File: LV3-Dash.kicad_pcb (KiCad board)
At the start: 2 copper layers, 88.9 x 50 mm, 95 parts, among them J1 Conn_01x05_MountingPin, J10 Conn_01x01, J2 USB_C_Receptacle_USB2.0_16P, J3 Conn_01x04_MountingPin, J4 MSD-11-A, J5 Conn_01x05_Pin, J7 62684-401100AHLF, J8 FTSH-105-01-L-DV-K-A, U1 STM32H743VITx, U2 TJA1051T-3, U3 AP3032KTR, U4 LMR51625YDDCR, U5 TLV74033PDBVR, U6 TLV74033PDBVR, Y1 Crystal_GND24

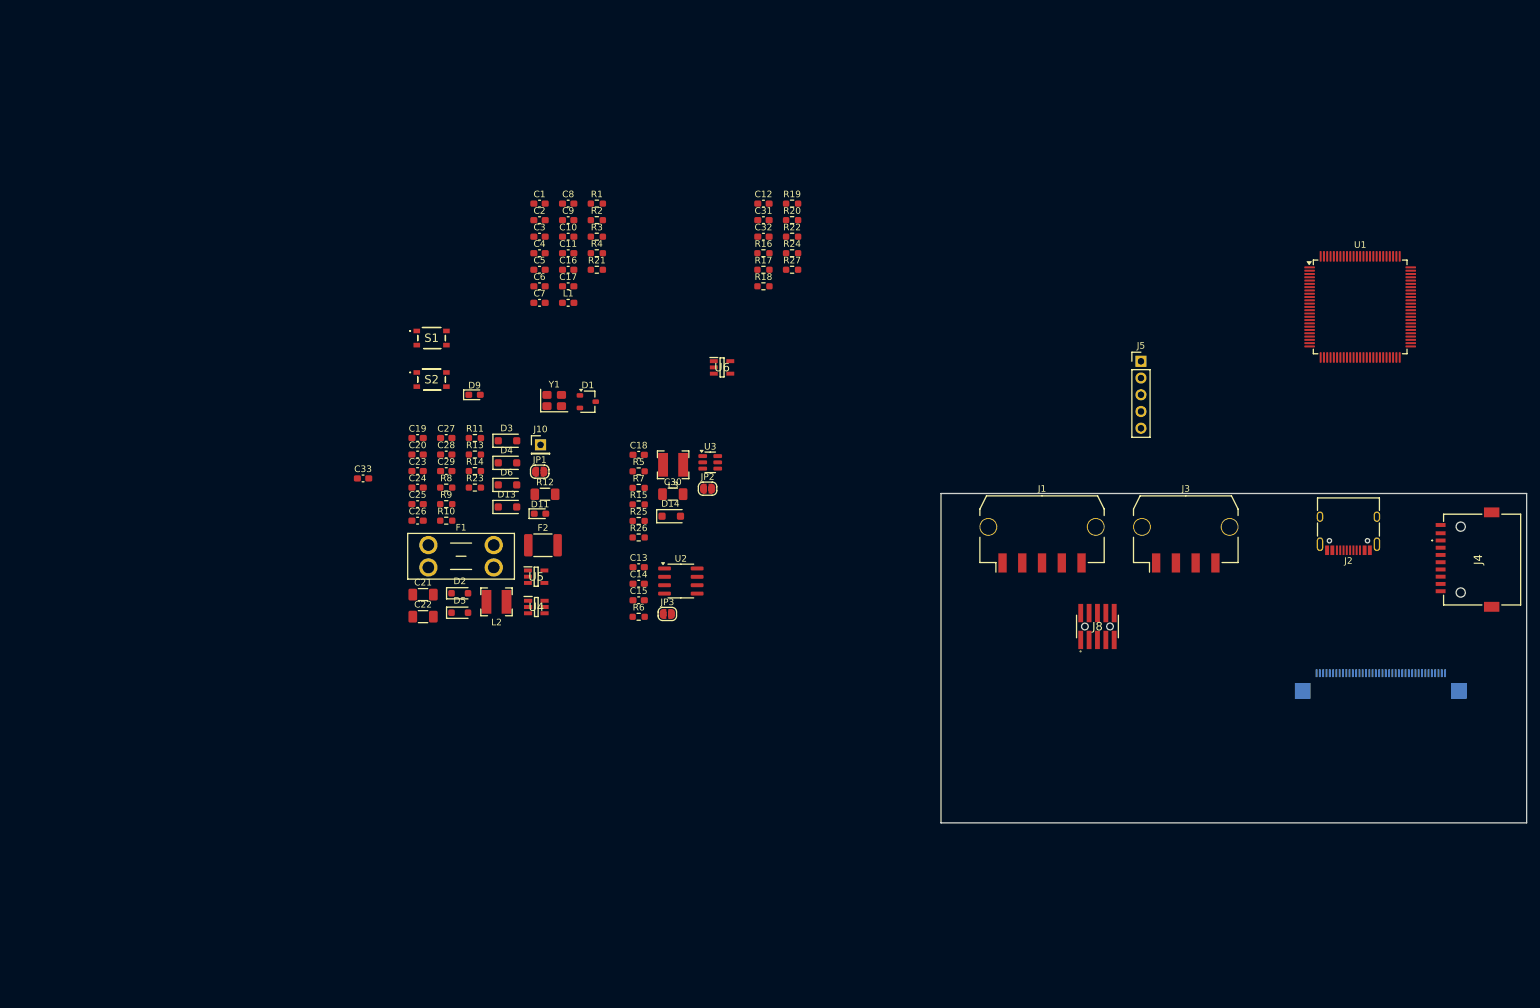
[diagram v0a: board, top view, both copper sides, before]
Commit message: initial dimensions and placement
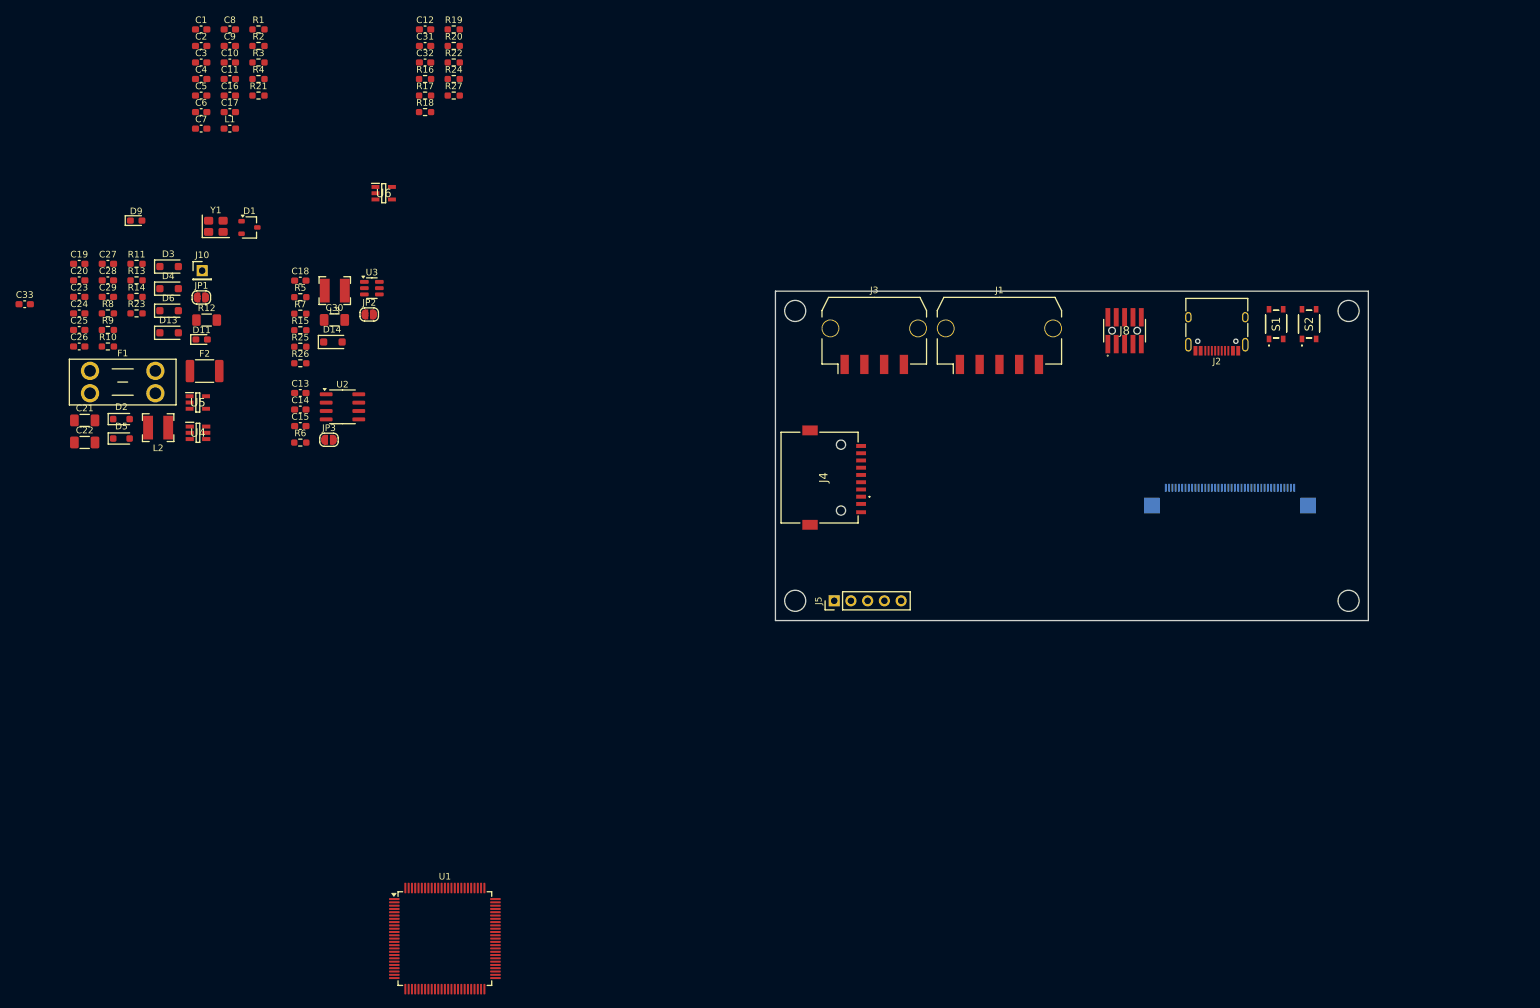
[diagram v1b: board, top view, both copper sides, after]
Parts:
- moved U1 168.8 mm to (99.8, 168.3)
- moved S2 133.5 mm to (231.0, 75.0), turned to 90 degrees
- moved S1 128.2 mm to (226.0, 75.0), turned to 90 degrees
- moved J4 100.9 mm to (156.9, 98.3), turned to -90 degrees
- moved J5 59.1 mm to (158.9, 117.0), turned to 90 degrees
- moved C11 57.8 mm to (67.2, 37.8)
- moved C12 57.8 mm to (96.8, 30.3)
- moved C14 57.8 mm to (77.9, 88.0)
- moved C8 57.8 mm to (67.2, 30.3)
- moved L1 57.8 mm to (67.2, 45.3)
- moved L2 57.8 mm to (56.3, 90.7)
- moved R13 57.8 mm to (53.0, 68.4)
- moved R16 57.8 mm to (96.8, 37.8)
- moved C10 57.8 mm to (67.2, 35.3)
- moved C13 57.8 mm to (77.9, 85.5)
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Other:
- board size 88.9 x 50 mm -> 90 x 50 mm

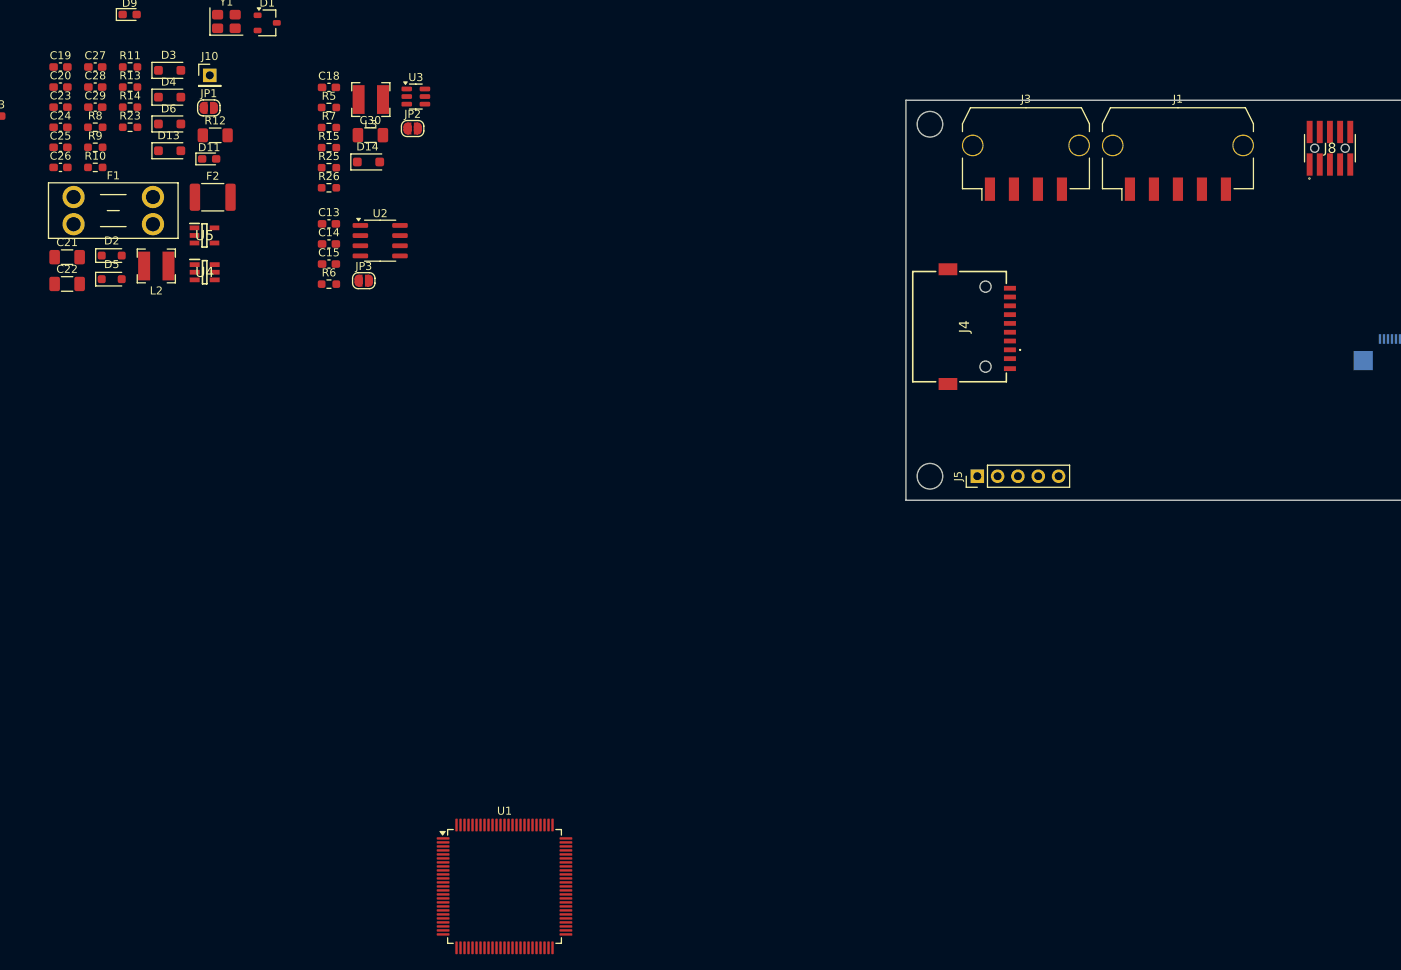
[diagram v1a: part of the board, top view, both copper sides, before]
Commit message: fix swd connector orientation, modify 12v input
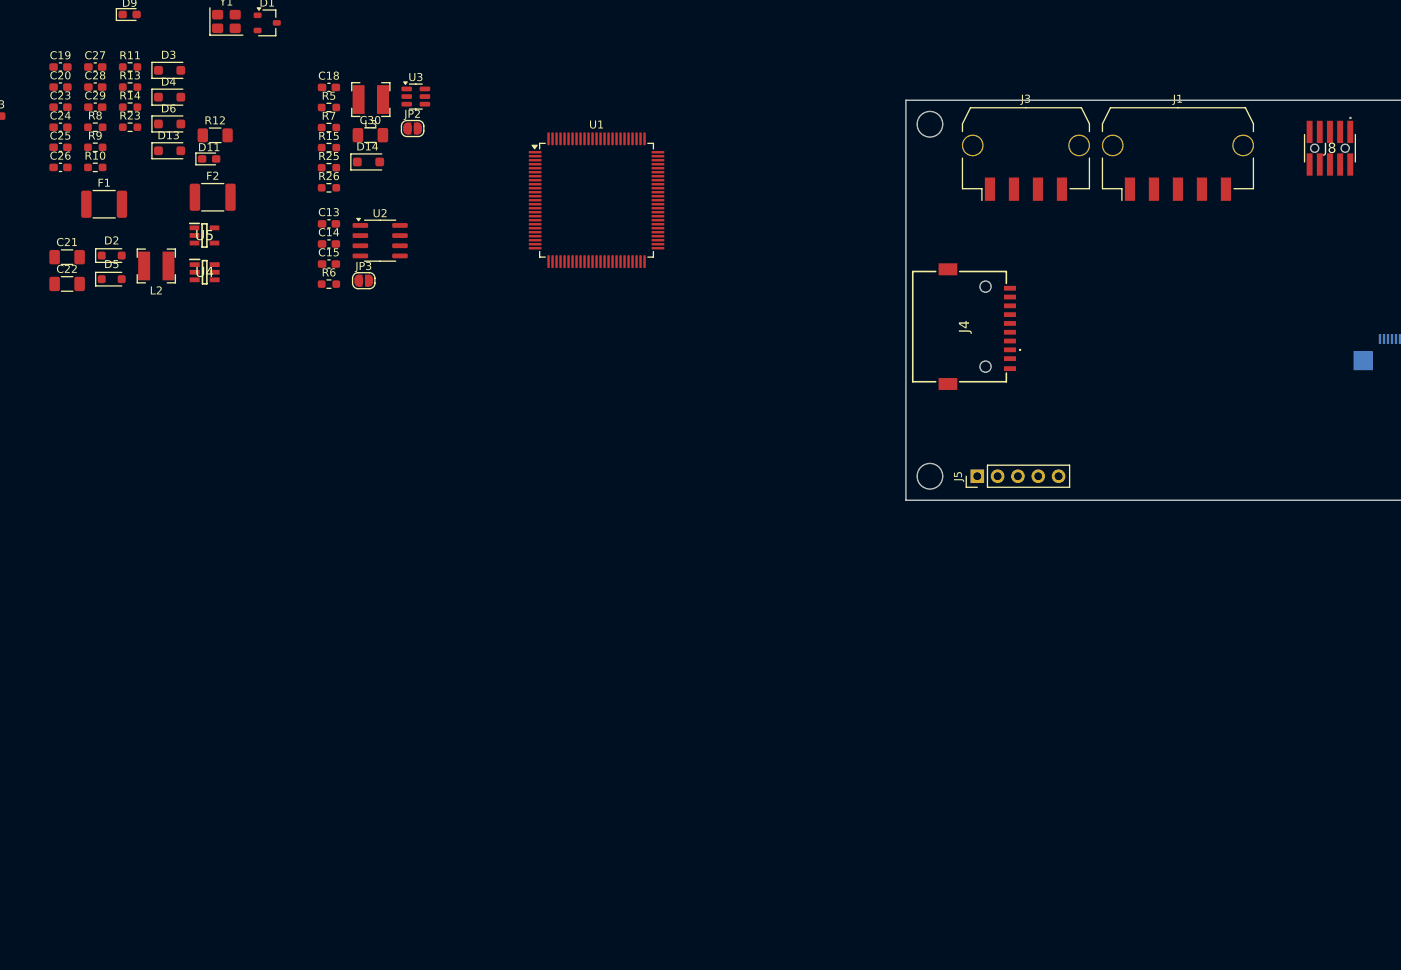
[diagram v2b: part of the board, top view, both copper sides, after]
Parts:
- removed J10: Conn_01x01, Connector_PinHeader_2.54mm:PinHeader_1x01_P2.54mm_Vertical
- removed JP1: SolderJumper_2_Open, Jumper:SolderJumper-2_P1.3mm_Open_RoundedPad1.0x1.5mm
- F1: value Fuse -> Polyfuse; footprint Fuse:Fuseholder_Blade_Mini_Keystone_3568 -> Fuse:Fuse_1812_4532Metric_Pad1.30x3.40mm_HandSolder
- moved U1 86.5 mm to (111.3, 82.5)
- moved F1 3.92 mm to (49.8, 83.0)
- turned J8 to 180 degrees
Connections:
- D13 pad 2: Net-(D13-A) -> +12V

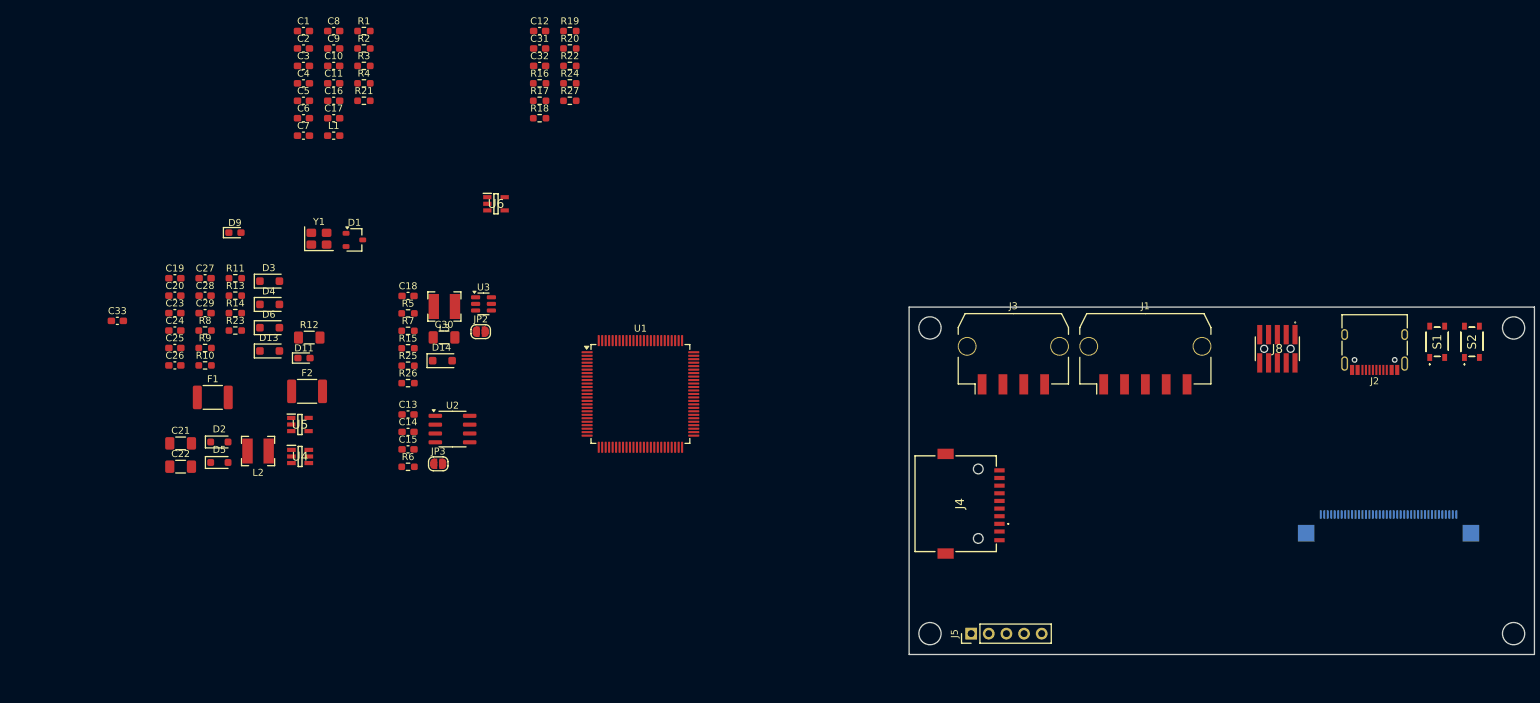
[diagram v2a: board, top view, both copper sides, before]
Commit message: basic layout organization, fix +VDDA typo
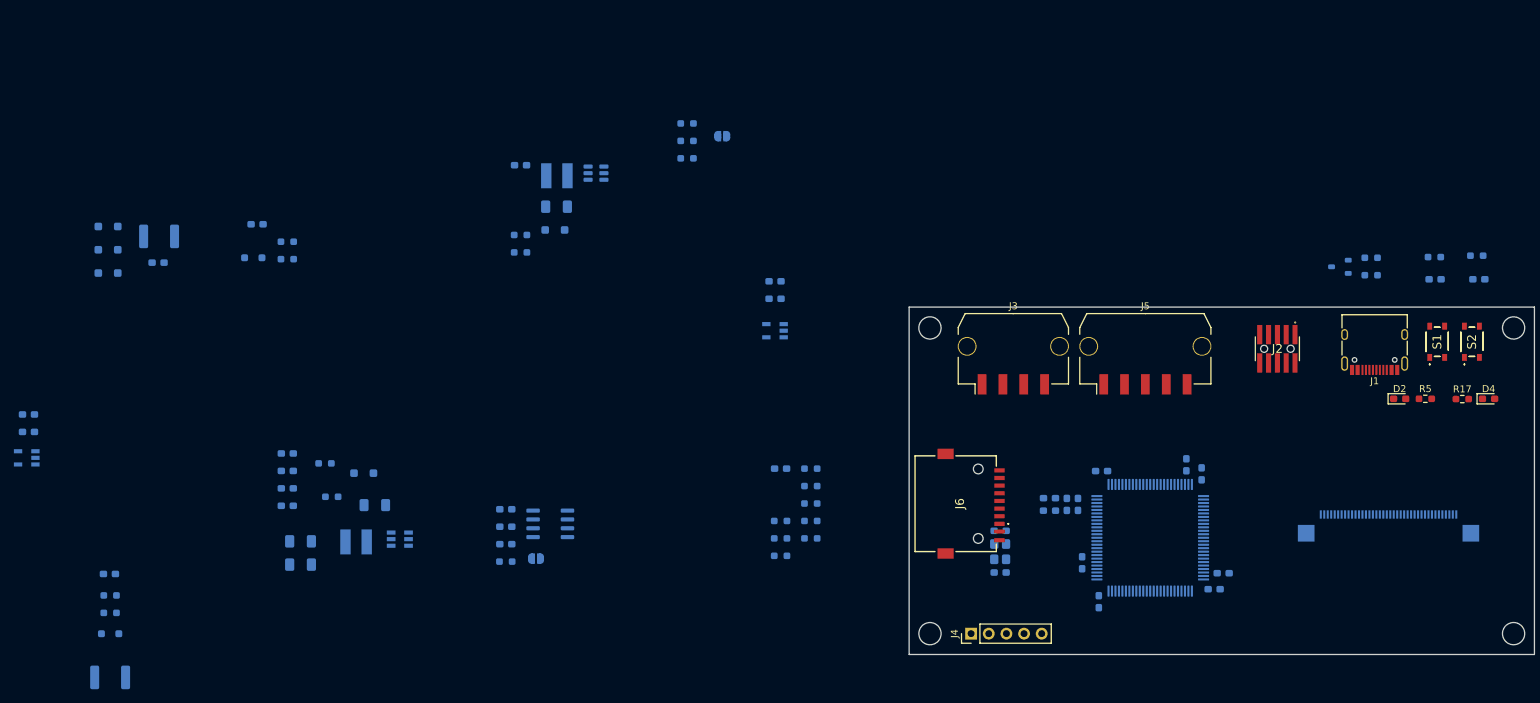
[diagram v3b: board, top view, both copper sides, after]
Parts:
- C1: renamed from C33; moved to B.Cu
- C10: renamed from C2; moved to B.Cu
- C11: renamed from C10; moved to B.Cu
- C12: renamed from C11; moved to B.Cu
- C13: renamed from C17; moved to B.Cu
- C14: renamed from C16; moved to B.Cu
- C15: renamed from C13; moved to B.Cu
- C16: renamed from C14; moved to B.Cu
- C17: renamed from C15; moved to B.Cu
- C18: renamed from C31; moved to B.Cu
- C19: renamed from C32; moved to B.Cu
- C2: renamed from C3; moved to B.Cu
- C20: renamed from C12; moved to B.Cu
- C21: renamed from C19; moved to B.Cu
- C22: renamed from C20; moved to B.Cu
- C23: renamed from C21; moved to B.Cu
- C24: renamed from C22; moved to B.Cu
- C25: renamed from C23; moved to B.Cu
- C26: renamed from C24; moved to B.Cu
- C27: renamed from C25; moved to B.Cu
- C28: renamed from C26; moved to B.Cu
- C29: renamed from C27; moved to B.Cu
- C3: renamed from C4; moved to B.Cu
- C30: renamed from C28; moved to B.Cu
- C31: renamed from C29; moved to B.Cu
- C32: renamed from C30; moved to B.Cu
- C33: renamed from C18; moved to B.Cu
- C4: renamed from C5; moved to B.Cu
- C5: renamed from C6; moved to B.Cu
- C6: renamed from C7; moved to B.Cu
- C7: renamed from C8; moved to B.Cu
- C8: renamed from C9; moved to B.Cu
- C9: renamed from C1; moved to B.Cu
- D1, F1, F2, JP2, L1, L2, L3, R1, R2, R3, R4, R6, U1, U2, U4, U5, Y1: moved to B.Cu
- D10: renamed from D14; moved to B.Cu
- D3: renamed from D2; moved to B.Cu
- D5: renamed from D13; moved to B.Cu
- D6: renamed from D3; moved to B.Cu
- D7: renamed from D4; moved to B.Cu
- D8: renamed from D5; moved to B.Cu
- D9: renamed from D6; moved to B.Cu
- JP1: renamed from JP3; moved to B.Cu
- R10: renamed from R19; moved to B.Cu
- R11: renamed from R20; moved to B.Cu
- R12: renamed from R22; moved to B.Cu
- R13: renamed from R24; moved to B.Cu
- R14: renamed from R27; moved to B.Cu
- R15: renamed from R8; moved to B.Cu
- R16: renamed from R9; moved to B.Cu
- R18: renamed from R10; moved to B.Cu
- R19: renamed from R11; moved to B.Cu
- R20: renamed from R12; moved to B.Cu
- R21: renamed from R13; moved to B.Cu
- R22: renamed from R14; moved to B.Cu
- R23: renamed from R26; moved to B.Cu
- R24: renamed from R25; moved to B.Cu
- R25: renamed from R7; moved to B.Cu
- R26: renamed from R5; moved to B.Cu
- R27: renamed from R15; moved to B.Cu
- R7: renamed from R16; moved to B.Cu
- R8: renamed from R17; moved to B.Cu
- R9: renamed from R18; moved to B.Cu
- U3: renamed from U6; moved to B.Cu
- U6: renamed from U3; moved to B.Cu
- moved R17 176.9 mm to (229.6, 83.2)
- moved D4 170.6 mm to (233.4, 83.2)
- moved D2 169.3 mm to (220.6, 83.2)
- moved C12 167.2 mm to (232.0, 66.0), turned to 180 degrees
- moved R2 162.9 mm to (231.7, 62.6), turned to 180 degrees
- moved C11 161.5 mm to (225.7, 66.0), turned to 180 degrees
- moved R5 158.7 mm to (224.3, 83.2)
- moved R1 157.5 mm to (225.6, 62.8), turned to 180 degrees
- moved C2 151.2 mm to (193.9, 110.6)
- moved R3 147.6 mm to (216.5, 62.9), turned to 180 degrees
- moved R4 147.6 mm to (216.5, 65.4), turned to 180 degrees
- moved C1 146.9 mm to (177.3, 112.4), turned to -90 degrees
- moved C14 145.0 mm to (195.2, 108.3)
- moved D1 141.9 mm to (212.0, 64.2), turned to 180 degrees
- moved C3 141.0 mm to (192.1, 94.0), turned to 90 degrees
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- renumbered D9 to D2, D11 to D4, J2 to J1, J8 to J2, J5 to J4, J1 to J5, J4 to J6, R23 to R17, R21 to R5
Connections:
- U1 pad 20: VDDA -> +VDDA
- U1 pad 21: VDDA -> +VDDA

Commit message: full preliminary layout
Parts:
- JP1: moved to F.Cu
- moved D3 147.6 mm to (180.1, 89.9), turned to -90 degrees
- moved C31 147.1 mm to (169.3, 105.9), turned to 0 degrees
- moved U5 147.0 mm to (169.6, 102.9), turned to -90 degrees
- moved C21 146.9 mm to (180.1, 86.2), turned to 90 degrees
- moved C30 146.8 mm to (169.3, 99.9), turned to 0 degrees
- moved F1 146.2 mm to (175.5, 82.9), turned to -90 degrees
- moved R15 145.6 mm to (178.4, 86.2), turned to -90 degrees
- moved R16 145.5 mm to (178.4, 89.6), turned to -90 degrees
- moved C33 144.0 mm to (231.1, 93.7), turned to 90 degrees
- moved L3 139.0 mm to (233.3, 88.0), turned to -90 degrees
- moved D10 138.7 mm to (233.4, 93.1), turned to 90 degrees
- moved R24 138.5 mm to (229.0, 91.0), turned to 0 degrees
- moved D9 136.6 mm to (169.2, 88.8), turned to 0 degrees
- moved C32 135.7 mm to (231.9, 84.0), turned to 0 degrees
- moved R23 134.8 mm to (226.9, 84.8), turned to 0 degrees
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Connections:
- U1 pad 51: unconnected-(U1-PB12-Pad51) -> FDCAN2_RX
- U1 pad 92: unconnected-(U1-PB6-Pad92) -> FDCAN2_TX
